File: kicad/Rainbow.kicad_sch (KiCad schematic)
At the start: 17 parts

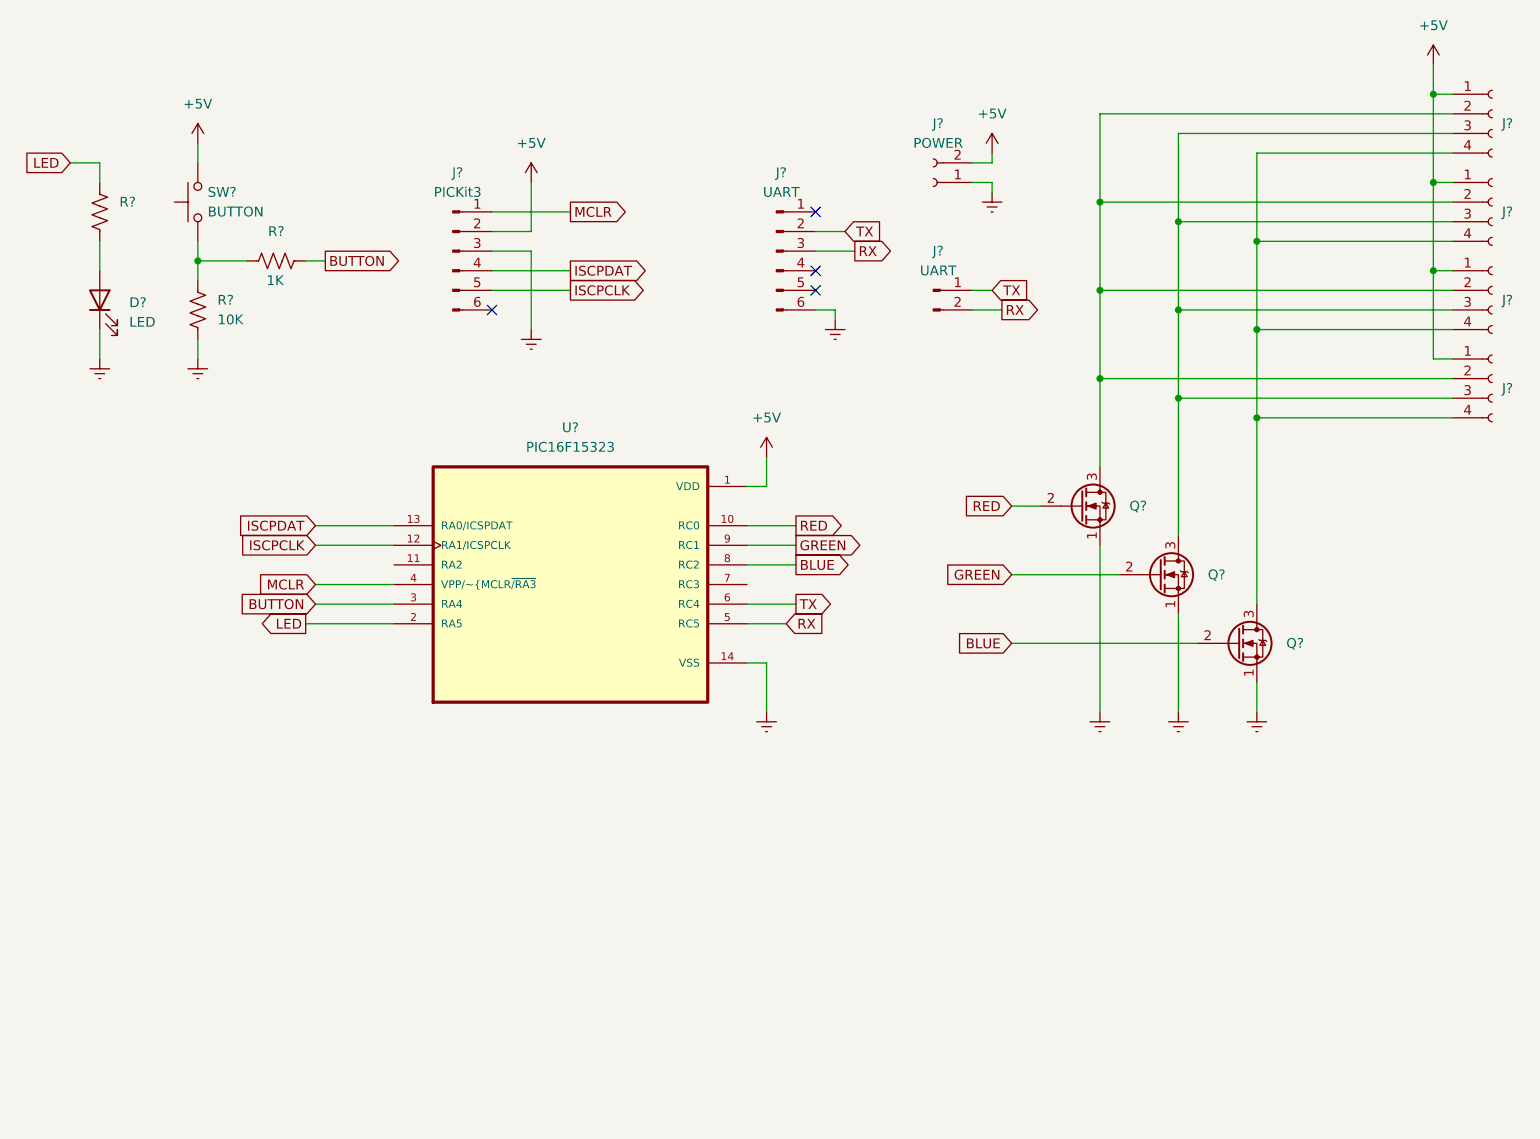
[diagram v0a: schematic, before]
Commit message: Schematic tweaks and untangle PCB ratsnest
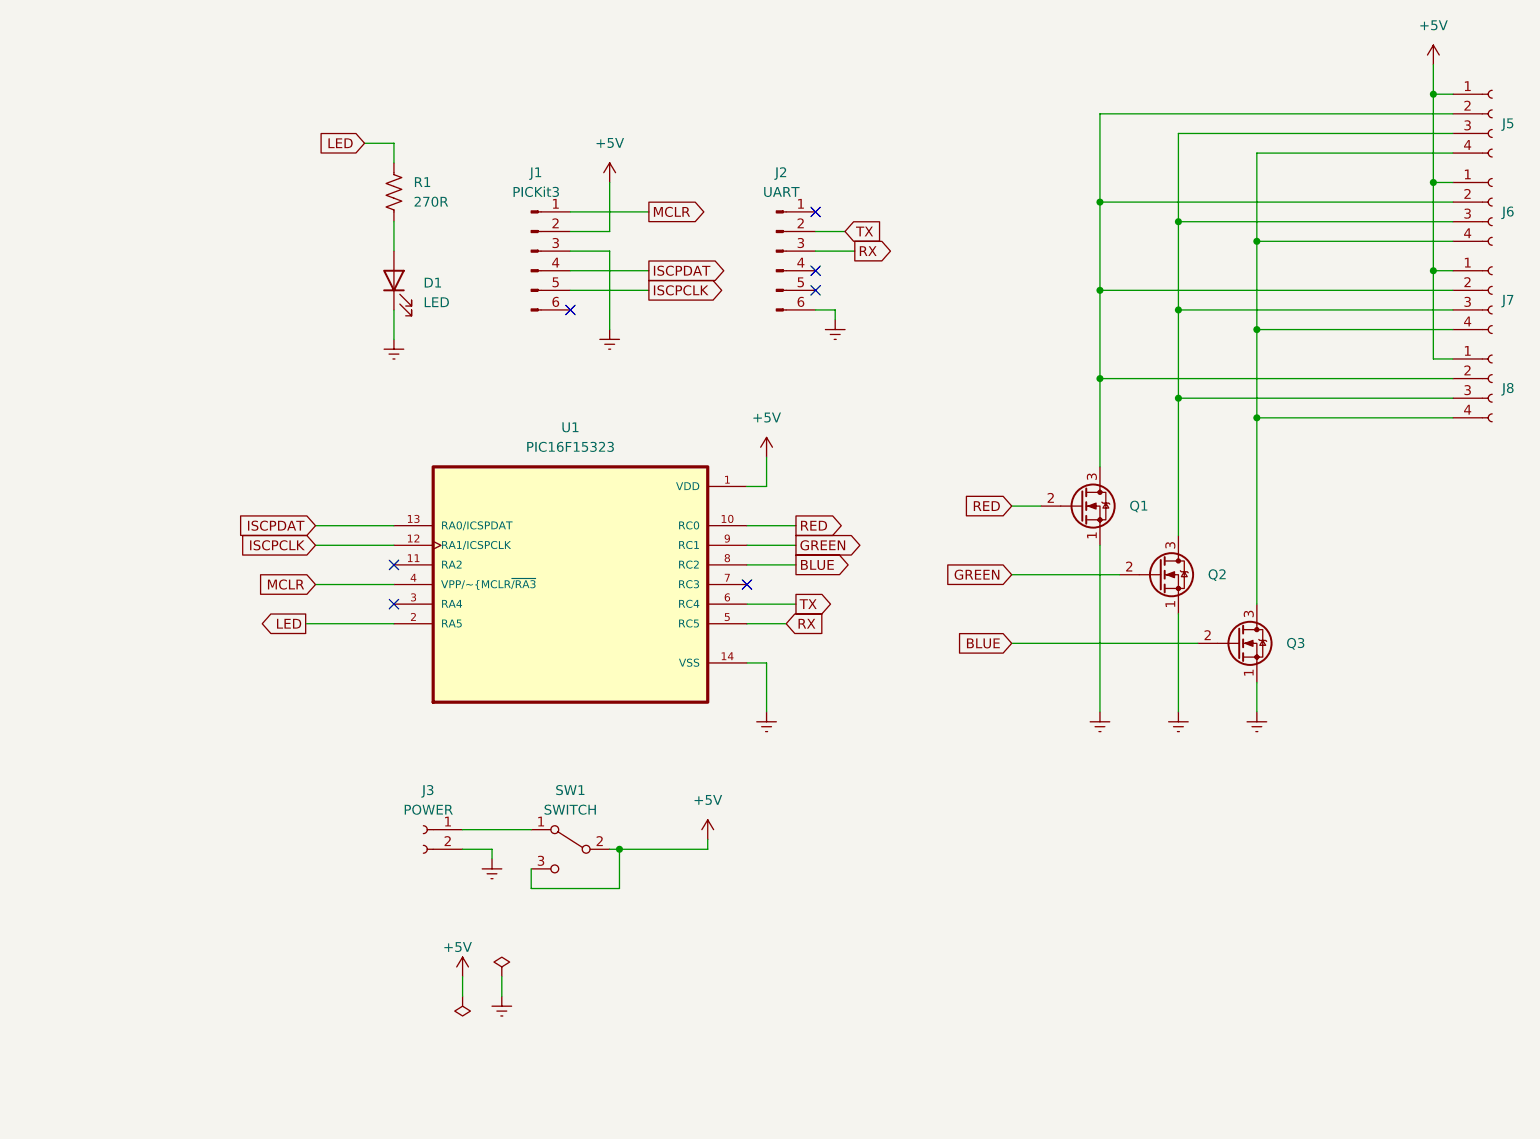
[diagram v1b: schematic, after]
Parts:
- removed J? (x3): Conn_01x04_Female, symbol Connector:Conn_01x04_Female
- removed J?: UART, symbol Connector:Conn_01x02_Male
- removed R?: 1K, symbol Device:R_US
- removed R?: 10K, symbol Device:R_US
- removed SW?: BUTTON, symbol Switch:SW_Push
- added J6, J7, J8: RGB, Connector_PinSocket_2.54mm:PinSocket_1x04_P2.54mm_Vertical, symbol Connector:Conn_01x04_Female
- added SW1: SWITCH, CK_Switch:CK_Switch, symbol Switch:SW_SPDT
- D1: renamed from D?; footprint (none) -> LED_THT:LED_D5.0mm
- J1, J2: renamed from J?; footprint (none) -> Connector_PinHeader_2.54mm:PinHeader_1x06_P2.54mm_Vertical
- J3: renamed from J?; footprint (none) -> Connector_PinSocket_2.54mm:PinSocket_1x02_P2.54mm_Vertical
- J5: renamed from J?; value Conn_01x04_Female -> RGB; footprint (none) -> Connector_PinSocket_2.54mm:PinSocket_1x04_P2.54mm_Vertical
- Q1, Q2, Q3: renamed from Q?; footprint Package_TO_SOT_THT:TO-92_W4.0mm_StaggerEven_Horizontal_FlatSideDown -> Package_TO_SOT_THT:TO-220-3_Vertical
- R1: renamed from R?; value R_US -> 270R; footprint (none) -> Resistor_THT:R_Axial_DIN0207_L6.3mm_D2.5mm_P7.62mm_Horizontal
- U1: renamed from U?; footprint SOIC127P600X175-14N -> Package_DIP:DIP-14_W7.62mm_Socket_LongPads
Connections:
- net +5V: now also J6.1 (Pin_1), J7.1 (Pin_1), J8.1 (Pin_1), SW1.2 (B), SW1.3 (C); no longer J3.2 (Pin_2)
- net GNDREF: now also J3.2 (Pin_2); no longer J3.1 (Pin_1)
- net at J5.2 (Pin_2), Q1.3 (D): now also J6.2 (Pin_2), J7.2 (Pin_2), J8.2 (Pin_2)
- net at J5.3 (Pin_3), Q2.3 (D): now also J6.3 (Pin_3), J7.3 (Pin_3), J8.3 (Pin_3)
- net at J5.4 (Pin_4), Q3.3 (D): now also J6.4 (Pin_4), J7.4 (Pin_4), J8.4 (Pin_4)
- net BUTTON: no longer names the net of U1.3 (RA4)
- new net: J3.1 (Pin_1), SW1.1 (A)
- no-connect marks 4 -> 7
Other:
- moved on the sheet: D1, J1, J3, R1

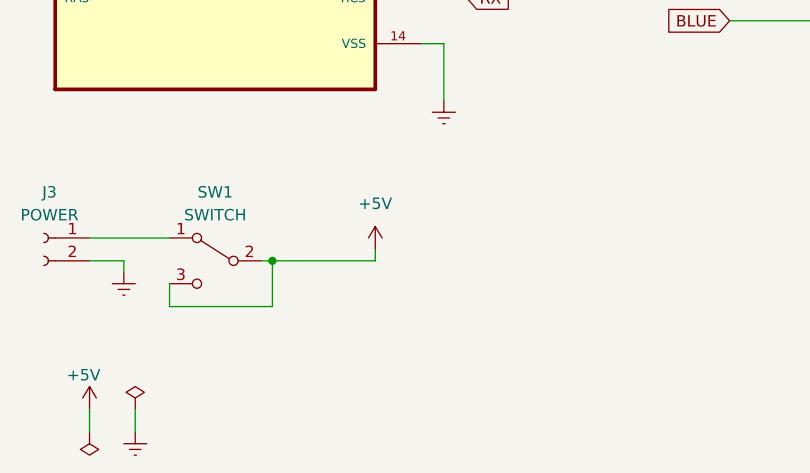
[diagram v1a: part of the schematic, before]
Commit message: Add capacitors to power supply
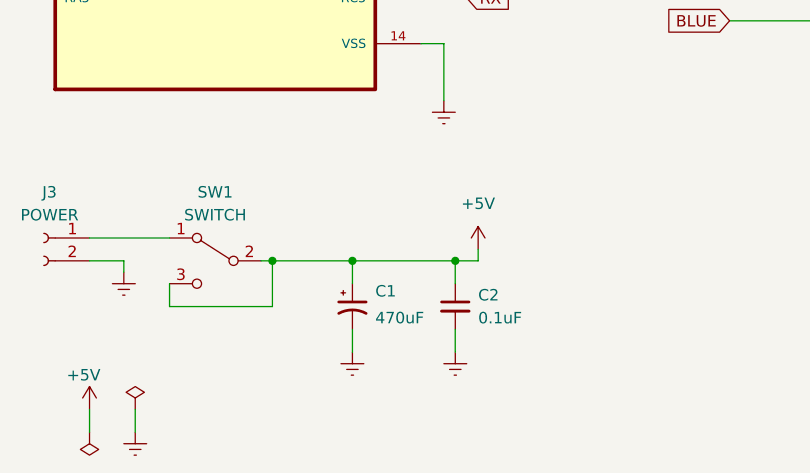
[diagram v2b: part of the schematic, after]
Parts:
- added C1: 470uF, Capacitor_THT:CP_Radial_D8.0mm_P3.50mm, symbol Device:C_Polarized_Small_US
- added C2: 0.1uF, Capacitor_THT:C_Disc_D4.3mm_W1.9mm_P5.00mm, symbol Device:C_Small
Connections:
- net +5V: now also C1.1, C2.1
- net GNDREF: now also C1.2, C2.2
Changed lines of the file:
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@@
 (kicad_sch (version 20211123) (generator eeschema)
   (paper "A4")
+  (junction (at 104.14 128.27) (diameter 0) (color 0 0 0 0)
+  )
   (junction (at 200.66 53.34) (diameter 0) (color 0 0 0 0)
   )
@@
   )
   (junction (at 157.48 44.45) (diameter 0) (color 0 0 0 0)
+  )
+  (junction (at 115.57 128.27) (diameter 0) (color 0 0 0 0)
   )
   (junction (at 177.8 60.96) (diameter 0) (color 0 0 0 0)
@@
     (stroke (width 0) (type default) (color 0 0 0 0))
   )
-  (wire (pts (xy 106.68 127) (xy 106.68 128.27))
+  (wire (pts (xy 118.11 127) (xy 118.11 128.27))
     (stroke (width 0) (type default) (color 0 0 0 0))
   )
@@
     (stroke (width 0) (type default) (color 0 0 0 0))
   )
+  (wire (pts (xy 115.57 135.89) (xy 115.57 138.43))
+    (stroke (width 0) (type default) (color 0 0 0 0))
+  )
   (wire (pts (xy 146.05 83.82) (xy 149.86 83.82))
     (stroke (width 0) (type default) (color 0 0 0 0))
@@
     (stroke (width 0) (type default) (color 0 0 0 0))
   )
+  (wire (pts (xy 115.57 128.27) (xy 104.14 128.27))
+    (stroke (width 0) (type default) (color 0 0 0 0))
+  )
   (wire (pts (xy 66.04 36.83) (xy 66.04 39.37))
     (stroke (width 0) (type default) (color 0 0 0 0))
@@
     (stroke (width 0) (type default) (color 0 0 0 0))
   )
+  (wire (pts (xy 104.14 135.89) (xy 104.14 138.43))
+    (stroke (width 0) (type default) (color 0 0 0 0))
+  )
   (wire (pts (xy 177.8 60.96) (xy 203.2 60.96))
     (stroke (width 0) (type default) (color 0 0 0 0))
@@
     (stroke (width 0) (type default) (color 0 0 0 0))
   )
+  (wire (pts (xy 104.14 128.27) (xy 104.14 130.81))
+    (stroke (width 0) (type default) (color 0 0 0 0))
+  )
   (wire (pts (xy 157.48 44.45) (xy 157.48 55.88))
     (stroke (width 0) (type default) (color 0 0 0 0))
@@
     (stroke (width 0) (type default) (color 0 0 0 0))
   )
+  (wire (pts (xy 104.14 128.27) (xy 95.25 128.27))
+    (stroke (width 0) (type default) (color 0 0 0 0))
+  )
+  (wire (pts (xy 115.57 128.27) (xy 115.57 130.81))
+    (stroke (width 0) (type default) (color 0 0 0 0))
+  )
   (wire (pts (xy 66.04 58.42) (xy 66.04 62.23))
     (stroke (width 0) (type default) (color 0 0 0 0))
@@
     (stroke (width 0) (type default) (color 0 0 0 0))
   )
-  (wire (pts (xy 106.68 128.27) (xy 95.25 128.27))
+  (wire (pts (xy 118.11 128.27) (xy 115.57 128.27))
     (stroke (width 0) (type default) (color 0 0 0 0))
   )
@@
     (pin "1")
   )
+  (symbol (lib_id "Device:C_Polarized_Small_US") (at 104.14 133.35 0) (unit 1)
+    (in_bom yes) (on_board yes)
+    (property "Reference" "C1" (id 0) (at 106.68 131.6481 0)
+      (effects (font (size 1.27 1.27)) (justify left))
+    )
+    (property "Value" "470uF" (id 1) (at 106.68 134.62 0)
+      (effects (font (size 1.27 1.27)) (justify left))
+    )
+    (property "Footprint" "Capacitor_THT:CP_Radial_D8.0mm_P3.50mm" (id 2) (at 104.14 133.35 0)
+      (effects (font (size 1.27 1.27)) hide)
+    )
+    (property "Datasheet" "~" (id 3) (at 104.14 133.35 0)
+      (effects (font (size 1.27 1.27)) hide)
+    )
+    (pin "1")
+    (pin "2")
+  )
   (symbol (lib_id "power:GNDREF") (at 93.98 60.96 0) (unit 1)
     (in_bom yes) (on_board yes) (fields_autoplaced)
@@
     )
     (pin "1")
+  )
+  (symbol (lib_id "Device:C_Small") (at 115.57 133.35 0) (unit 1)
+    (in_bom yes) (on_board yes) (fields_autoplaced)
+    (property "Reference" "C2" (id 0) (at 118.11 132.0862 0)
+      (effects (font (size 1.27 1.27)) (justify left))
+    )
+    (property "Value" "0.1uF" (id 1) (at 118.11 134.6262 0)
+      (effects (font (size 1.27 1.27)) (justify left))
+    )
+    (property "Footprint" "Capacitor_THT:C_Disc_D4.3mm_W1.9mm_P5.00mm" (id 2) (at 115.57 133.35 0)
+      (effects (font (size 1.27 1.27)) hide)
+    )
+    (property "Datasheet" "~" (id 3) (at 115.57 133.35 0)
+      (effects (font (size 1.27 1.27)) hide)
+    )
+    (pin "1")
+    (pin "2")
   )
   (symbol (lib_id "Connector:Conn_01x02_Female") (at 69.85 125.73 0) (mirror y) (unit 1)
@@
     (pin "2")
     (pin "3")
+  )
+  (symbol (lib_id "power:GNDREF") (at 115.57 138.43 0) (mirror y) (unit 1)
+    (in_bom yes) (on_board yes) (fields_autoplaced)
+    (property "Reference" "#PWR03" (id 0) (at 115.57 144.78 0)
+      (effects (font (size 1.27 1.27)) hide)
+    )
+    (property "Value" "GNDREF" (id 1) (at 115.57 143.51 0)
+      (effects (font (size 1.27 1.27)) hide)
+    )
+    (property "Footprint" "" (id 2) (at 115.57 138.43 0)
+      (effects (font (size 1.27 1.27)) hide)
+    )
+    (property "Datasheet" "" (id 3) (at 115.57 138.43 0)
+      (effects (font (size 1.27 1.27)) hide)
+    )
+    (pin "1")
   )
   (symbol (lib_id "Connector:Conn_01x04_Female") (at 208.28 67.31 0) (unit 1)
@@
     (pin "1")
   )
-  (symbol (lib_id "power:+5V") (at 106.68 127 0) (mirror y) (unit 1)
-    (in_bom yes) (on_board yes) (fields_autoplaced)
-    (property "Reference" "#PWR09" (id 0) (at 106.68 130.81 0)
-      (effects (font (size 1.27 1.27)) hide)
-    )
-    (property "Value" "+5V" (id 1) (at 106.68 121.92 0))
-    (property "Footprint" "" (id 2) (at 106.68 127 0)
-      (effects (font (size 1.27 1.27)) hide)
-    )
-    (property "Datasheet" "" (id 3) (at 106.68 127 0)
+  (symbol (lib_id "power:+5V") (at 118.11 127 0) (mirror y) (unit 1)
+    (in_bom yes) (on_board yes) (fields_autoplaced)
+    (property "Reference" "#PWR09" (id 0) (at 118.11 130.81 0)
+      (effects (font (size 1.27 1.27)) hide)
+    )
+    (property "Value" "+5V" (id 1) (at 118.11 121.92 0))
+    (property "Footprint" "" (id 2) (at 118.11 127 0)
+      (effects (font (size 1.27 1.27)) hide)
+    )
+    (property "Datasheet" "" (id 3) (at 118.11 127 0)
       (effects (font (size 1.27 1.27)) hide)
     )
@@
     (pin "6")
   )
+  (symbol (lib_id "power:GNDREF") (at 104.14 138.43 0) (mirror y) (unit 1)
+    (in_bom yes) (on_board yes) (fields_autoplaced)
+    (property "Reference" "#PWR02" (id 0) (at 104.14 144.78 0)
+      (effects (font (size 1.27 1.27)) hide)
+    )
+    (property "Value" "GNDREF" (id 1) (at 104.14 143.51 0)
+      (effects (font (size 1.27 1.27)) hide)
+    )
+    (property "Footprint" "" (id 2) (at 104.14 138.43 0)
+      (effects (font (size 1.27 1.27)) hide)
+    )
+    (property "Datasheet" "" (id 3) (at 104.14 138.43 0)
+      (effects (font (size 1.27 1.27)) hide)
+    )
+    (pin "1")
+  )
   (symbol (lib_id "Connector:Conn_01x04_Female") (at 208.28 44.45 0) (unit 1)
     (in_bom yes) (on_board yes) (fields_autoplaced)
@@
       (reference "#PWR01") (unit 1) (value "GNDREF") (footprint "")
     )
+    (path "/d0696f3b-2839-4a84-9673-60bc752d8957"
+      (reference "#PWR02") (unit 1) (value "GNDREF") (footprint "")
+    )
+    (path "/b08ba4b2-e7b8-45b4-9304-1cb9233187d4"
+      (reference "#PWR03") (unit 1) (value "GNDREF") (footprint "")
+    )
     (path "/890826dd-df00-4020-9370-1e0062111fe4"
       (reference "#PWR04") (unit 1) (value "+5V") (footprint "")
@@
       (reference "#PWR0103") (unit 1) (value "+5V") (footprint "")
     )
+    (path "/8ab3c0b4-3e09-4b9f-8242-15c09eeeb9e0"
+      (reference "C1") (unit 1) (value "470uF") (footprint "Capacitor_THT:CP_Radial_D8.0mm_P3.50mm")
+    )
+    (path "/a0c99c13-0855-443a-89fd-04bf8395f39b"
+      (reference "C2") (unit 1) (value "0.1uF") (footprint "Capacitor_THT:C_Disc_D4.3mm_W1.9mm_P5.00mm")
+    )
     (path "/ebab1235-9ca0-40c8-93dc-5ee3f6f863d8"

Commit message: A bunch of stuff
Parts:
- removed U1: PIC16F15323, Package_DIP:DIP-14_W7.62mm_Socket_LongPads, symbol PIC16F15323:PIC16F15323
- added J4: JACK, Connector_BarrelJack:BarrelJack_Horizontal, symbol Connector:Barrel_Jack
- added J9: SOURCE, Connector_PinHeader_2.54mm:PinHeader_1x03_P2.54mm_Vertical, symbol Connector:Conn_01x03_Male
- added U1: PIC16F15325, Package_DIP:DIP-14_W7.62mm_Socket_LongPads, symbol PIC16F15325:PIC16F15325
- J3: value POWER -> JUMPER
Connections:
- net +5V: now also U1.1 (VDD)
- net BLUE: now also U1.8 (RC2)
- net GNDREF: now also J4.2, U1.14 (VSS)
- net GREEN: now also U1.9 (RC1)
- net ISCPCLK: now also U1.12 (RA1/ICSPCLK)
- net ISCPDAT: now also U1.13 (RA0/ICSPDAT)
- net LED: now also U1.2 (RA5)
- net MCLR: now also U1.4 (VPP/~{MCLR~{/RA3})
- net RED: now also U1.10 (RC0)
- net RX: now also U1.5 (RC5)
- net TX: now also U1.6 (RC4)
- net at J3.1 (Pin_1): now also J9.3 (Pin_3); no longer SW1.1 (A)
- new net: J9.2 (Pin_2), SW1.1 (A)
- new net: J4.1, J9.1 (Pin_1)
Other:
- moved on the sheet: C1, C2, J3, SW1

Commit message: Finish PCB
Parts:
- removed J4: JACK, Connector_BarrelJack:BarrelJack_Horizontal, symbol Connector:Barrel_Jack
- added H1, H2, H3, H4: MountingHole, MountingHole:MountingHole_2.1mm, symbol Mechanical:MountingHole
- added J4: JACK, Tensility_Barrel_Jack:Tensility_Barrel_Jack, symbol Tensility_Barrel_Jack:Tensility_Barrel_Jack
- J2: value UART -> USB SERIAL
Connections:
- net BLUE: now also U1.10 (RC0); no longer U1.8 (RC2)
- net GNDREF: now also J4.2, J4.3
- net RED: now also U1.8 (RC2); no longer U1.10 (RC0)
- net at J9.1 (Pin_1): now also J4.1
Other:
- moved on the sheet: C1, C2, J3, J9, SW1

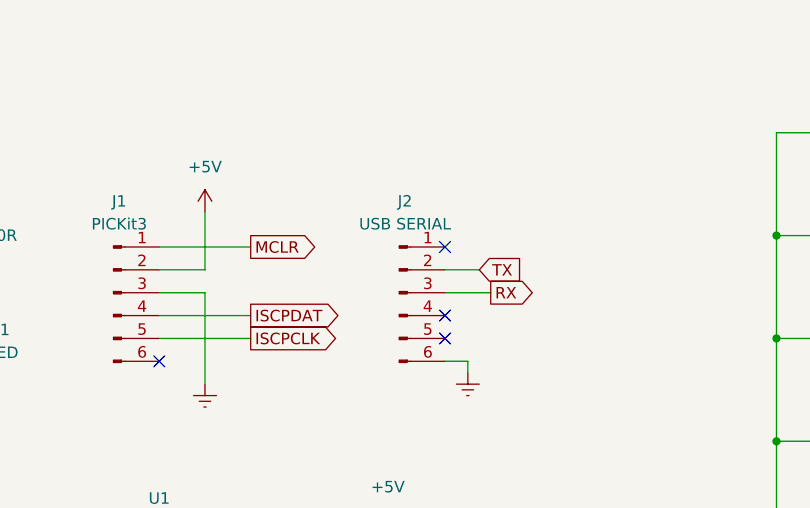
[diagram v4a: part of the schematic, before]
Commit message: tweak silk and placement
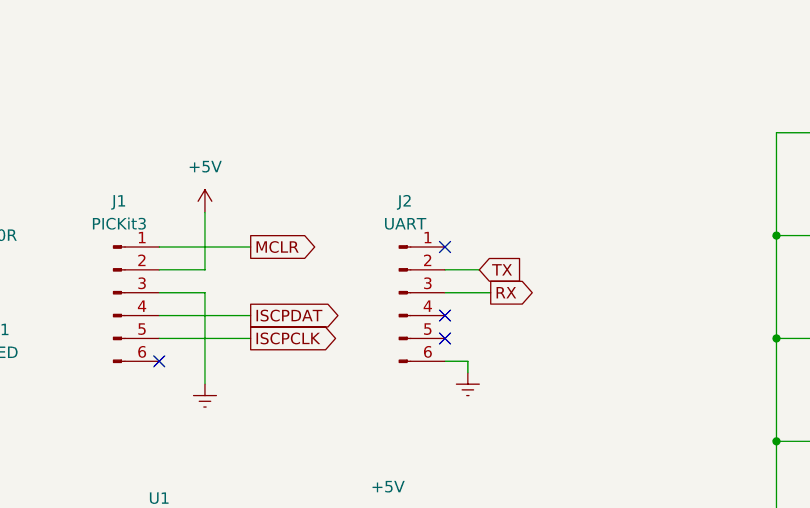
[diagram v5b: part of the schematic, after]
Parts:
- J2: value USB SERIAL -> UART
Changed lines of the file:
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@@
     (in_bom yes) (on_board yes) (fields_autoplaced)
     (property "Reference" "J2" (id 0) (at 116.205 40.64 0))
-    (property "Value" "USB SERIAL" (id 1) (at 116.205 43.18 0))
+    (property "Value" "UART" (id 1) (at 116.205 43.18 0))
     (property "Footprint" "Connector_PinHeader_2.54mm:PinHeader_1x06_P2.54mm_Vertical" (id 2) (at 115.57 50.8 0)
       (effects (font (size 1.27 1.27)) hide)
@@
     )
     (path "/c2db2e9b-18cc-4503-9689-b5fe3ce87c52"
-      (reference "J2") (unit 1) (value "USB SERIAL") (footprint "Connector_PinHeader_2.54mm:PinHeader_1x06_P2.54mm_Vertical")
+      (reference "J2") (unit 1) (value "UART") (footprint "Connector_PinHeader_2.54mm:PinHeader_1x06_P2.54mm_Vertical")
     )
     (path "/a21b73ca-fae1-410e-a604-b8b2a0adc85d"
